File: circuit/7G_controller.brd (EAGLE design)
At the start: 66.3 x 72 mm, 22 parts, among them Q1 32768Hz, T1 TPS1101D

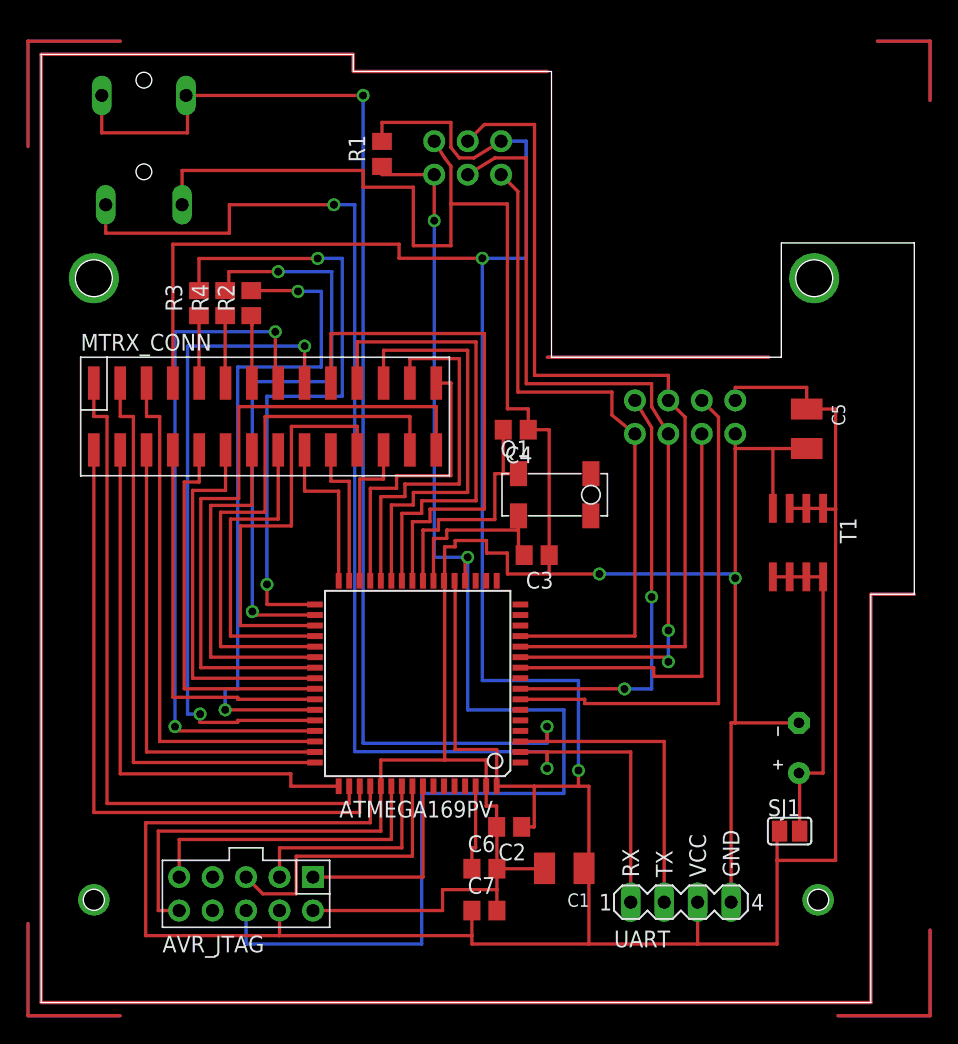
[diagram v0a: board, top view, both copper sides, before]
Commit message: 
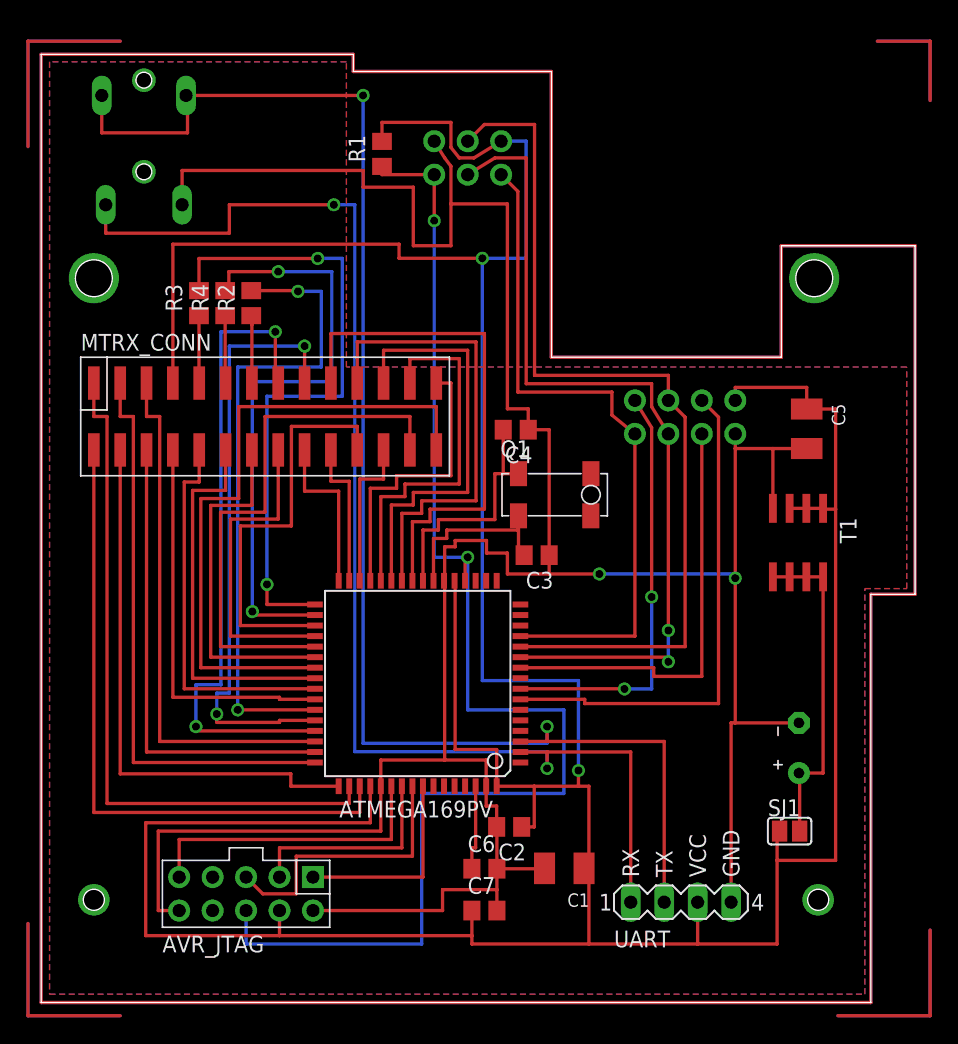
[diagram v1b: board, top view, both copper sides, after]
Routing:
- net N$1: track 209.0 -> 293.7 mm
- net N$19: track 209.0 -> 293.7 mm
- net N$7: track 16.8 -> 0.00 mm
- net N$5: track 16.8 -> 0.00 mm
- net L9: track 50.1 -> 45.7 mm
- net L8: track 52.7 -> 49.5 mm
- net CAPS: track 51.3 -> 49.4 mm
- added copper zone on layer 16, net N$23
- added copper zone on layer 1, net N$24
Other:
- board size 66.3 x 72 mm -> 66.4 x 72 mm
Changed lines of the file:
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@@
 <setting verticaltext="up"/>
 </settings>
-<grid distance="0.0125" unitdist="inch" unit="mm" style="lines" multiple="1" display="yes" altdistance="0.025" altunitdist="inch" altunit="inch"/>
+<grid distance="0.05" unitdist="inch" unit="inch" style="lines" multiple="1" display="yes" altdistance="0.025" altunitdist="inch" altunit="inch"/>
 <layers>
 <layer number="1" name="Top" color="4" fill="1" visible="yes" active="yes"/>
@@
 <layer number="43" name="vRestrict" color="2" fill="10" visible="no" active="yes"/>
 <layer number="44" name="Drills" color="7" fill="1" visible="no" active="yes"/>
-<layer number="45" name="Holes" color="7" fill="1" visible="no" active="yes"/>
+<layer number="45" name="Holes" color="7" fill="1" visible="yes" active="yes"/>
 <layer number="46" name="Milling" color="3" fill="1" visible="no" active="yes"/>
 <layer number="47" name="Measures" color="7" fill="1" visible="no" active="yes"/>
@@
 <wire x1="0" y1="0" x2="63" y2="0" width="0" layer="20"/>
 <wire x1="63" y1="0" x2="63" y2="31" width="0" layer="20"/>
-<wire x1="63" y1="31" x2="66.3" y2="31" width="0" layer="20"/>
-<wire x1="66.3" y1="31" x2="66.3" y2="57.6825" width="0" layer="20"/>
-<wire x1="66.3" y1="57.6825" x2="56.2025" y2="57.6825" width="0" layer="20"/>
-<wire x1="56.2025" y1="57.6825" x2="56.2025" y2="49" width="0" layer="20"/>
+<wire x1="63" y1="31" x2="66.3575" y2="31" width="0" layer="20"/>
+<wire x1="66.3575" y1="31" x2="66.3575" y2="57.4675" width="0" layer="20"/>
+<wire x1="66.3575" y1="57.4675" x2="56.2025" y2="57.4675" width="0" layer="20"/>
+<wire x1="56.2025" y1="57.4675" x2="56.2025" y2="49" width="0" layer="20"/>
 <wire x1="56.2025" y1="49" x2="38.75" y2="49" width="0" layer="20"/>
 <wire x1="38.75" y1="49" x2="38.75" y2="70.7" width="0" layer="20"/>
@@
 <wire x1="67.5" y1="73" x2="67.5" y2="68.5" width="0.254" layer="16"/>
 </signal>
-<signal name="N$7">
-<wire x1="38.4325" y1="49" x2="55.25" y2="49" width="0.254" layer="16"/>
-</signal>
 <signal name="N$1">
 <wire x1="0" y1="0" x2="0" y2="72" width="0.254" layer="16"/>
 <wire x1="0" y1="72" x2="23.7" y2="72" width="0.254" layer="16"/>
 <wire x1="23.7" y1="72" x2="23.7" y2="70.7" width="0.254" layer="16"/>
-<wire x1="23.7" y1="70.7" x2="38.4325" y2="70.7" width="0.254" layer="16"/>
-<wire x1="66.3" y1="31" x2="63" y2="31" width="0.254" layer="16"/>
+<wire x1="23.7" y1="70.7" x2="38.75" y2="70.7" width="0.254" layer="16"/>
+<wire x1="66.3575" y1="31" x2="63" y2="31" width="0.254" layer="16"/>
 <wire x1="63" y1="31" x2="63" y2="0" width="0.254" layer="16"/>
 <wire x1="63" y1="0" x2="0" y2="0" width="0.254" layer="16"/>
-</signal>
-<signal name="N$5">
-<wire x1="38.4325" y1="49" x2="55.25" y2="49" width="0.254" layer="1"/>
+<wire x1="38.735" y1="49" x2="38.735" y2="70.7" width="0.254" layer="16"/>
+<wire x1="38.75" y1="49" x2="56.2025" y2="49" width="0.254" layer="16"/>
+<wire x1="56.1975" y1="49" x2="56.1975" y2="57.4675" width="0.254" layer="16"/>
+<wire x1="56.1975" y1="57.4675" x2="66.3575" y2="57.4675" width="0.254" layer="16"/>
+<wire x1="66.3575" y1="57.4675" x2="66.3575" y2="31" width="0.254" layer="16"/>
+<wire x1="38.75" y1="49" x2="38.735" y2="49" width="0" layer="19" extent="16-16"/>
+<wire x1="38.75" y1="70.7" x2="38.735" y2="70.7" width="0" layer="19" extent="16-16"/>
 </signal>
 <signal name="N$19">
@@
 <wire x1="0" y1="72" x2="23.7" y2="72" width="0.254" layer="1"/>
 <wire x1="23.7" y1="72" x2="23.7" y2="70.7" width="0.254" layer="1"/>
-<wire x1="23.7" y1="70.7" x2="38.4325" y2="70.7" width="0.254" layer="1"/>
-<wire x1="66.3" y1="31" x2="63" y2="31" width="0.254" layer="1"/>
+<wire x1="23.7" y1="70.7" x2="38.735" y2="70.7" width="0.254" layer="1"/>
+<wire x1="66.3575" y1="31" x2="63" y2="31" width="0.254" layer="1"/>
 <wire x1="63" y1="31" x2="63" y2="0" width="0.254" layer="1"/>
 <wire x1="63" y1="0" x2="0" y2="0" width="0.254" layer="1"/>
+<wire x1="38.735" y1="70.7" x2="38.735" y2="49" width="0.254" layer="1"/>
+<wire x1="38.735" y1="48.9966" x2="56.1975" y2="48.9966" width="0.254" layer="1"/>
+<wire x1="56.1975" y1="48.9966" x2="56.1975" y2="57.4675" width="0.254" layer="1"/>
+<wire x1="56.1975" y1="57.4675" x2="66.3575" y2="57.4675" width="0.254" layer="1"/>
+<wire x1="66.3575" y1="57.4675" x2="66.3575" y2="31" width="0.254" layer="1"/>
 </signal>
 <signal name="H28">
@@
 <contactref element="ATMEGA169PV" pad="42"/>
 <wire x1="10" y1="41.96" x2="10" y2="23.1775" width="0.254" layer="1"/>
-<wire x1="20.79" y1="23.025" x2="14.9225" y2="23.025" width="0.254" layer="1"/>
-<wire x1="14.9225" y1="23.025" x2="14.9225" y2="23.1775" width="0.254" layer="1"/>
-<wire x1="14.9225" y1="23.1775" x2="10" y2="23.1775" width="0.254" layer="1"/>
+<wire x1="20.79" y1="23.025" x2="18.0975" y2="23.025" width="0.254" layer="1"/>
+<wire x1="18.0975" y1="23.025" x2="18.0975" y2="23.1775" width="0.254" layer="1"/>
+<wire x1="18.0975" y1="23.1775" x2="10" y2="23.1775" width="0.254" layer="1"/>
 </signal>
 <signal name="N$2">
@@
 <wire x1="17.78" y1="47.04" x2="17.78" y2="50.935" width="0.254" layer="1"/>
 <via x="17.78" y="50.935" extent="1-16" drill="0.6" shape="square"/>
-<wire x1="17.78" y1="50.935" x2="10.16" y2="50.935" width="0.254" layer="16"/>
-<wire x1="10.16" y1="50.935" x2="10.16" y2="20.955" width="0.254" layer="16"/>
-<via x="10.16" y="20.955" extent="1-16" drill="0.6" shape="square"/>
-<wire x1="10.16" y1="20.955" x2="10.16" y2="20.625" width="0.254" layer="1"/>
-<wire x1="10.16" y1="20.625" x2="20.79" y2="20.625" width="0.254" layer="1"/>
+<wire x1="17.78" y1="50.935" x2="13.6525" y2="50.935" width="0.254" layer="16"/>
+<wire x1="13.6525" y1="50.935" x2="13.6525" y2="24.13" width="0.254" layer="16"/>
+<wire x1="13.6525" y1="24.13" x2="11.7475" y2="24.13" width="0.254" layer="16"/>
+<wire x1="11.7475" y1="24.13" x2="11.7475" y2="20.955" width="0.254" layer="16"/>
+<via x="11.7475" y="20.955" extent="1-16" drill="0.6" shape="square"/>
+<wire x1="11.7475" y1="20.955" x2="11.7475" y2="20.625" width="0.254" layer="1"/>
+<wire x1="11.7475" y1="20.625" x2="20.79" y2="20.625" width="0.254" layer="1"/>
 </signal>
 <signal name="L9">
@@
 <wire x1="20.0025" y1="47.04" x2="20.0025" y2="49.8475" width="0.254" layer="1"/>
 <via x="20.0025" y="49.8475" extent="1-16" drill="0.6" shape="square"/>
-<wire x1="20.0025" y1="49.8475" x2="11.1125" y2="49.8475" width="0.254" layer="16"/>
-<wire x1="11.1125" y1="49.8475" x2="11.1125" y2="21.9075" width="0.254" layer="16"/>
-<wire x1="11.1125" y1="21.9075" x2="12.065" y2="21.9075" width="0.254" layer="16"/>
-<via x="12.065" y="21.9075" extent="1-16" drill="0.6" shape="square"/>
-<wire x1="20.79" y1="21.425" x2="14.9225" y2="21.425" width="0.254" layer="1"/>
-<wire x1="14.9225" y1="21.425" x2="14.9225" y2="21.2725" width="0.254" layer="1"/>
-<wire x1="14.9225" y1="21.2725" x2="12.065" y2="21.2725" width="0.254" layer="1"/>
-<wire x1="12.065" y1="21.2725" x2="12.065" y2="21.9075" width="0.254" layer="1"/>
+<wire x1="20.0025" y1="49.8475" x2="14.2875" y2="49.8475" width="0.254" layer="16"/>
+<wire x1="14.2875" y1="49.8475" x2="14.2875" y2="23.495" width="0.254" layer="16"/>
+<wire x1="14.2875" y1="23.495" x2="13.335" y2="23.495" width="0.254" layer="16"/>
+<wire x1="13.335" y1="23.495" x2="13.335" y2="21.9075" width="0.254" layer="16"/>
+<via x="13.335" y="21.9075" extent="1-16" drill="0.6" shape="square"/>
+<wire x1="20.79" y1="21.425" x2="18.0975" y2="21.425" width="0.254" layer="1"/>
+<wire x1="18.0975" y1="21.425" x2="18.0975" y2="21.2725" width="0.254" layer="1"/>
+<wire x1="18.0975" y1="21.2725" x2="13.335" y2="21.2725" width="0.254" layer="1"/>
+<wire x1="13.335" y1="21.2725" x2="13.335" y2="21.9075" width="0.254" layer="1"/>
 </signal>
 <signal name="L10">
@@
 <contactref element="ATMEGA169PV" pad="43"/>
 <wire x1="21.2725" y1="54" x2="21.2725" y2="48.26" width="0.254" layer="16"/>
-<via x="13.97" y="22.225" extent="1-16" drill="0.6" shape="square"/>
-<wire x1="13.97" y1="22.225" x2="20.79" y2="22.225" width="0.254" layer="1"/>
+<via x="14.9225" y="22.225" extent="1-16" drill="0.6" shape="square"/>
+<wire x1="14.9225" y1="22.225" x2="20.79" y2="22.225" width="0.254" layer="1"/>
 <wire x1="15.9512" y1="54.06" x2="19.5" y2="54.06" width="0.254" layer="1"/>
 <wire x1="19.5" y1="54.06" x2="19.5" y2="54" width="0.254" layer="1"/>
@@
 <wire x1="19.5" y1="54" x2="21.2725" y2="54" width="0.254" layer="16"/>
 <wire x1="21.2725" y1="48.26" x2="14.9225" y2="48.26" width="0.254" layer="16"/>
-<wire x1="14.9225" y1="48.26" x2="14.9225" y2="23.8125" width="0.254" layer="16"/>
-<wire x1="14.9225" y1="23.8125" x2="13.97" y2="23.8125" width="0.254" layer="16"/>
-<wire x1="13.97" y1="23.8125" x2="13.97" y2="22.225" width="0.254" layer="16"/>
+<wire x1="14.9225" y1="48.26" x2="14.9225" y2="22.225" width="0.254" layer="16"/>
 </signal>
 <signal name="SCRL">
@@
 <wire x1="36.245" y1="33.9725" x2="36.245" y2="36.96" width="0.254" layer="1"/>
 </signal>
+<signal name="N$23">
+<polygon width="0.254" layer="16" isolate="0.8128">
+<vertex x="0.635" y="0.635"/>
+<vertex x="62.5475" y="0.635"/>
+<vertex x="62.5475" y="31.4325"/>
+<vertex x="65.7225" y="31.4325"/>
+<vertex x="65.7225" y="48.26"/>
+<vertex x="23.1775" y="48.26"/>
+<vertex x="23.1775" y="71.4375"/>
+<vertex x="0.635" y="71.4375"/>
+</polygon>
+</signal>
+<signal name="N$24">
+<polygon width="0.254" layer="1" isolate="0.8128">
+<vertex x="0.635" y="0.635"/>
+<vertex x="62.5475" y="0.635"/>
+<vertex x="62.5475" y="31.4325"/>
+<vertex x="65.7225" y="31.4325"/>
+<vertex x="65.7225" y="48.26"/>
+<vertex x="23.1775" y="48.26"/>
+<vertex x="23.1775" y="71.4375"/>
+<vertex x="0.635" y="71.4375"/>
+</polygon>
+</signal>
+<signal name="N$25">
+<via x="7.8" y="70.04" extent="1-16" drill="1.2"/>
+<via x="7.8" y="63.08" extent="1-16" drill="1.2"/>
+<wire x1="7.8" y1="63.08" x2="7.8" y2="70.04" width="0" layer="19" extent="1-1"/>
+</signal>
 </signals>

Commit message: 
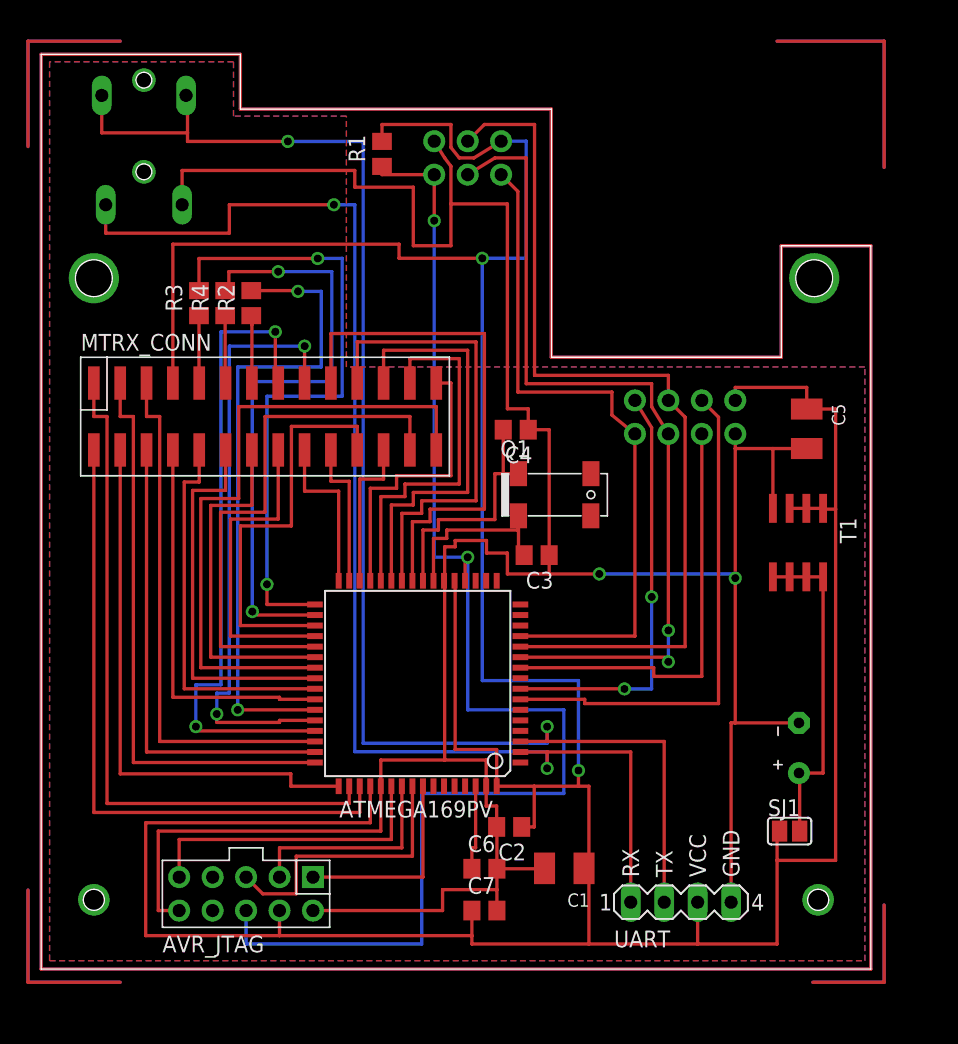
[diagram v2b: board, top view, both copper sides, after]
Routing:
- net N$1: track 293.7 -> 281.8 mm
- net N$19: track 293.7 -> 281.9 mm
- net N$18: track 8.50 -> 17.7 mm
- net N$12: track 8.50 -> 17.7 mm
- net N$30: track 114.4 -> 111.5 mm
- net N$17: track 13.5 -> 11.3 mm
- net N$11: track 13.5 -> 11.3 mm
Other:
- board size 66.4 x 72 mm -> 63 x 69.5 mm
